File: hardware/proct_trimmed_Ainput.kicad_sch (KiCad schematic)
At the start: 2 parts

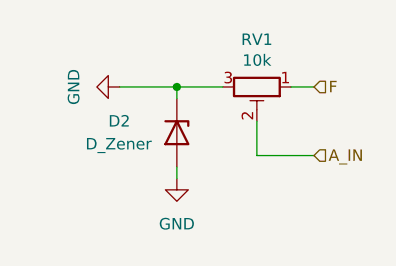
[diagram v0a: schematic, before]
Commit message: update to use latest kmlib; needs revision for connectors and ground inputs on analog inputs
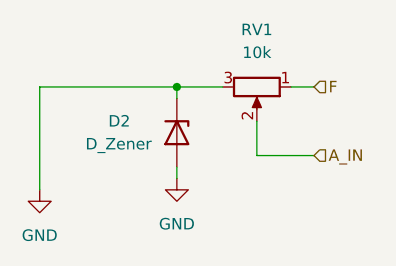
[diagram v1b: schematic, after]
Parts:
- removed RV1: 10k, Potentiometer_THT:Potentiometer_Bourns_3266W_Vertical, symbol BREAD_Slice-rescue:R_POT_TRIM-Device
- added RV1: 10k, Potentiometer_THT:Potentiometer_Bourns_3266W_Vertical, symbol Device:R_Potentiometer
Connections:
- net A_IN: now also RV1.2
- net F: now also RV1.1
- net GND: now also RV1.3
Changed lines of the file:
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@@
+	(wire
+		(pts
+			(xy 91.44 76.2) (xy 91.44 87.63)
+		)
+		(stroke
+			(width 0)
+			(type default)
+		)
+	)
 	(wire
 		(pts
@@
 	(wire
 		(pts
-			(xy 106.68 76.2) (xy 100.33 76.2)
+			(xy 106.68 76.2) (xy 91.44 76.2)
 		)
 		(stroke
@@
 	)
 	(symbol
-		(lib_id "BREAD_Slice-rescue:R_POT_TRIM-Device")
-		(at 115.57 76.2 270)
+		(lib_id "power:GND")
+		(at 91.44 87.63 0)
 		(unit 1)
 		(exclude_from_sim no)
@@
 		(on_board yes)
 		(dnp no)
-		(property "Reference" "RV1"
-			(at 115.57 70.9422 90)
-			(effects
-				(font
-					(size 1.27 1.27)
-				)
-			)
-		)
-		(property "Value" "10k"
-			(at 115.57 73.2536 90)
-			(effects
-				(font
-					(size 1.27 1.27)
-				)
-			)
-		)
-		(property "Footprint" "Potentiometer_THT:Potentiometer_Bourns_3266W_Vertical"
-			(at 115.57 76.2 0)
-			(effects
-				(font
-					(size 1.27 1.27)
-				)
-				(hide yes)
-			)
-		)
-		(property "Datasheet" "~"
-			(at 115.57 76.2 0)
-			(effects
-				(font
-					(size 1.27 1.27)
-				)
-				(hide yes)
-			)
-		)
-		(property "Description" ""
-			(at 115.57 76.2 0)
+		(property "Reference" "#PWR014"
+			(at 91.44 93.98 0)
+			(effects
+				(font
+					(size 1.27 1.27)
+				)
+				(hide yes)
+			)
+		)
+		(property "Value" "GND"
+			(at 91.44 92.71 0)
+			(effects
+				(font
+					(size 1.27 1.27)
+				)
+			)
+		)
+		(property "Footprint" ""
+			(at 91.44 87.63 0)
+			(effects
+				(font
+					(size 1.27 1.27)
+				)
+				(hide yes)
+			)
+		)
+		(property "Datasheet" ""
+			(at 91.44 87.63 0)
+			(effects
+				(font
+					(size 1.27 1.27)
+				)
+				(hide yes)
+			)
+		)
+		(property "Description" "Power symbol creates a global label with name \"GND\" , ground"
+			(at 91.44 87.63 0)
 			(effects
 				(font
@@
 		)
 		(pin "1"
-		)
-		(pin "2"
-		)
-		(pin "3"
 		)
 		(instances
 			(project "BREAD_Slice"
 				(path "/66043bca-a260-4915-9fce-8a51d324c687/b5da4b94-97ce-4ae4-aac7-1d4139497e7a"
-					(reference "RV4")
+					(reference "#PWR014")
 					(unit 1)
 				)
 				(path "/66043bca-a260-4915-9fce-8a51d324c687/b8c88354-25c1-41b8-b883-b077a970c54f"
-					(reference "RV3")
+					(reference "#PWR014")
 					(unit 1)
 				)
 				(path "/66043bca-a260-4915-9fce-8a51d324c687/c0d18fba-c059-4c8a-9412-a4a9c75bf00d"
-					(reference "RV2")
+					(reference "#PWR014")
 					(unit 1)
 				)
 				(path "/66043bca-a260-4915-9fce-8a51d324c687/d9371660-1998-461a-acc9-6e12c1d0530e"
-					(reference "RV1")
-					(unit 1)
-				)
-			)
-		)
-	)
-	(symbol
-		(lib_id "power:GND")
-		(at 100.33 76.2 270)
-		(unit 1)
-		(exclude_from_sim no)
-		(in_bom yes)
-		(on_board yes)
-		(dnp no)
-		(property "Reference" "#PWR016"
-			(at 93.98 76.2 0)
-			(effects
-				(font
-					(size 1.27 1.27)
-				)
-				(hide yes)
-			)
-		)
-		(property "Value" "GND"
-			(at 95.25 76.2 0)
-			(effects
-				(font
-					(size 1.27 1.27)
-				)
-			)
-		)
-		(property "Footprint" ""
-			(at 100.33 76.2 0)
-			(effects
-				(font
-					(size 1.27 1.27)
-				)
-				(hide yes)
-			)
-		)
-		(property "Datasheet" ""
-			(at 100.33 76.2 0)
-			(effects
-				(font
-					(size 1.27 1.27)
-				)
-				(hide yes)
-			)
-		)
-		(property "Description" ""
-			(at 100.33 76.2 0)
-			(effects
-				(font
-					(size 1.27 1.27)
-				)
-				(hide yes)
-			)
-		)
-		(pin "1"
-		)
-		(instances
-			(project "BREAD_Slice"
-				(path "/66043bca-a260-4915-9fce-8a51d324c687/b5da4b94-97ce-4ae4-aac7-1d4139497e7a"
-					(reference "#PWR022")
-					(unit 1)
-				)
-				(path "/66043bca-a260-4915-9fce-8a51d324c687/b8c88354-25c1-41b8-b883-b077a970c54f"
-					(reference "#PWR020")
-					(unit 1)
-				)
-				(path "/66043bca-a260-4915-9fce-8a51d324c687/c0d18fba-c059-4c8a-9412-a4a9c75bf00d"
-					(reference "#PWR018")
-					(unit 1)
-				)
-				(path "/66043bca-a260-4915-9fce-8a51d324c687/d9371660-1998-461a-acc9-6e12c1d0530e"
-					(reference "#PWR016")
+					(reference "#PWR014")
 					(unit 1)
 				)
@@
 		(on_board yes)
 		(dnp no)
-		(property "Reference" "#PWR017"
+		(property "Reference" "#PWR015"
 			(at 106.68 92.71 0)
 			(effects
@@
 			)
 		)
-		(property "Description" ""
+		(property "Description" "Power symbol creates a global label with name \"GND\" , ground"
 			(at 106.68 86.36 0)
 			(effects
@@
 			(project "BREAD_Slice"
 				(path "/66043bca-a260-4915-9fce-8a51d324c687/b5da4b94-97ce-4ae4-aac7-1d4139497e7a"
-					(reference "#PWR023")
+					(reference "#PWR021")
 					(unit 1)
 				)
 				(path "/66043bca-a260-4915-9fce-8a51d324c687/b8c88354-25c1-41b8-b883-b077a970c54f"
-					(reference "#PWR021")
+					(reference "#PWR019")
 					(unit 1)
 				)
 				(path "/66043bca-a260-4915-9fce-8a51d324c687/c0d18fba-c059-4c8a-9412-a4a9c75bf00d"
-					(reference "#PWR019")
+					(reference "#PWR017")
 					(unit 1)
 				)
 				(path "/66043bca-a260-4915-9fce-8a51d324c687/d9371660-1998-461a-acc9-6e12c1d0530e"
-					(reference "#PWR017")
+					(reference "#PWR015")
 					(unit 1)
 				)
@@
 			)
 		)
-		(property "Description" ""
+		(property "Description" "Zener diode"
 			(at 106.68 81.28 0)
 			(effects
@@
 					(unit 1)
 				)
+			)
+		)
+	)
+	(symbol
+		(lib_id "Device:R_Potentiometer")
+		(at 115.57 76.2 270)
+		(unit 1)
+		(exclude_from_sim no)
+		(in_bom yes)
+		(on_board yes)
+		(dnp no)
+		(fields_autoplaced yes)
+		(property "Reference" "RV1"
+			(at 115.57 69.85 90)
+			(effects
+				(font
+					(size 1.27 1.27)
+				)
+			)
+		)
+		(property "Value" "10k"
+			(at 115.57 72.39 90)
+			(effects
+				(font
+					(size 1.27 1.27)
+				)
+			)
+		)
+		(property "Footprint" "Potentiometer_THT:Potentiometer_Bourns_3266W_Vertical"
+			(at 115.57 76.2 0)
+			(effects
+				(font
+					(size 1.27 1.27)
+				)
+				(hide yes)
+			)
+		)
+		(property "Datasheet" "~"
+			(at 115.57 76.2 0)
+			(effects
+				(font
+					(size 1.27 1.27)
+				)
+				(hide yes)
+			)
+		)
+		(property "Description" "Potentiometer"
+			(at 115.57 76.2 0)
+			(effects
+				(font
+					(size 1.27 1.27)
+				)
+				(hide yes)
+			)
+		)
+		(pin "2"
+		)
+		(pin "3"
+		)
+		(pin "1"
+		)
+		(instances
+			(project ""
+				(path "/66043bca-a260-4915-9fce-8a51d324c687/b5da4b94-97ce-4ae4-aac7-1d4139497e7a"
+					(reference "RV4")
+					(unit 1)
+				)
+				(path "/66043bca-a260-4915-9fce-8a51d324c687/b8c88354-25c1-41b8-b883-b077a970c54f"
+					(reference "RV3")
+					(unit 1)
+				)
+				(path "/66043bca-a260-4915-9fce-8a51d324c687/c0d18fba-c059-4c8a-9412-a4a9c75bf00d"
+					(reference "RV2")
+					(unit 1)
+				)
+				(path "/66043bca-a260-4915-9fce-8a51d324c687/d9371660-1998-461a-acc9-6e12c1d0530e"
+					(reference "RV1")
+					(unit 1)
+				)
